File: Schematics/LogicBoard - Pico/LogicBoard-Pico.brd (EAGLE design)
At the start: 104.7 x 99.1 mm, 9 parts

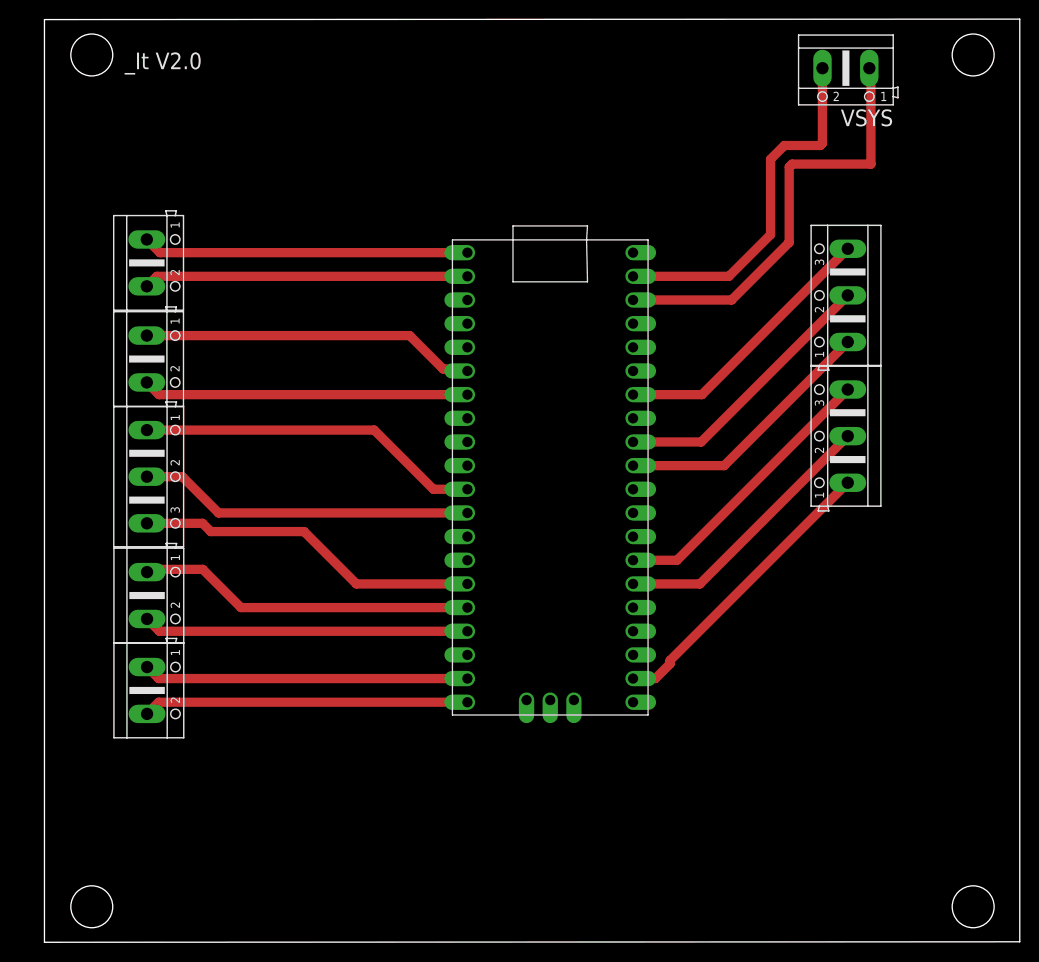
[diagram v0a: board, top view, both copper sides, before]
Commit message: Refactored Power PCB
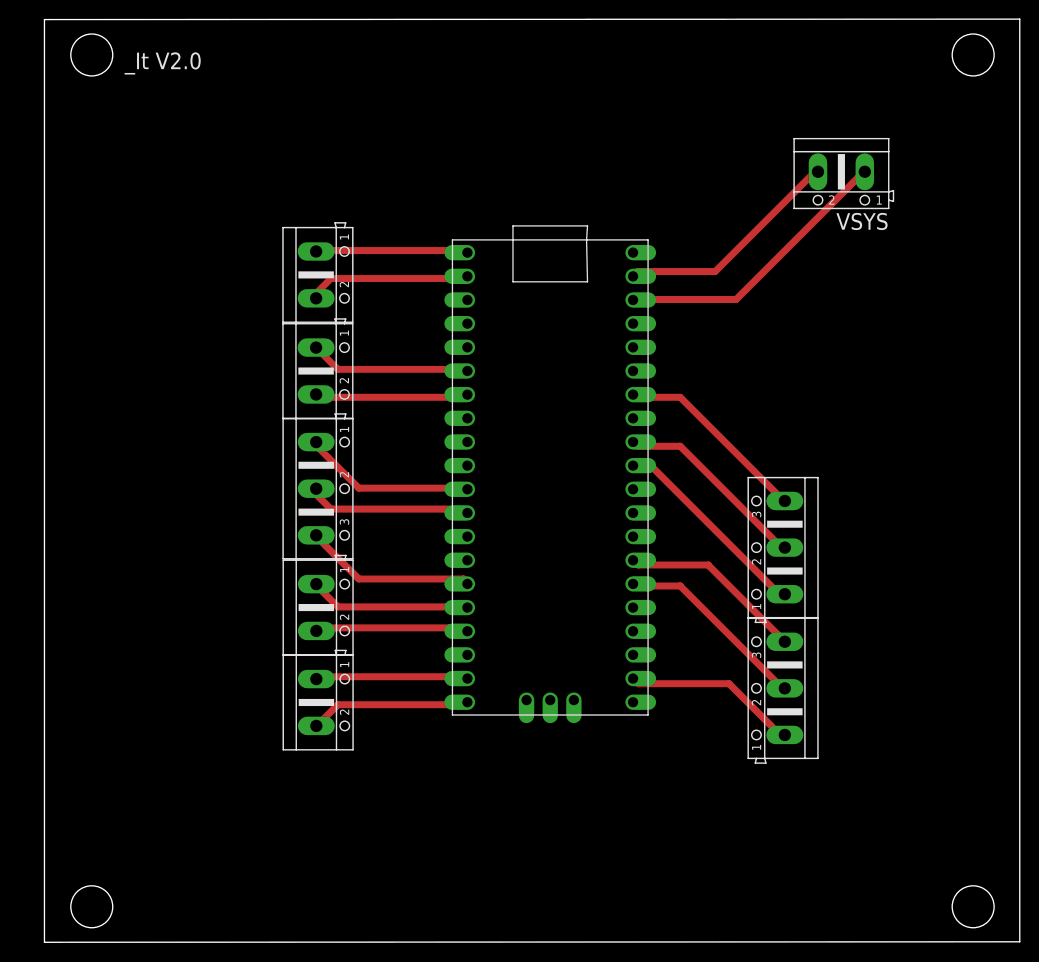
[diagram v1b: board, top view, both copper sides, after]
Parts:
- moved I2C1 27.9 mm to (79.5, 27.3)
- moved ADC 27.9 mm to (79.5, 42.4)
- moved PWM_M1 18.2 mm to (29.2, 25.7)
- moved PWM_M2 18.2 mm to (29.2, 35.9)
- moved PWM_SERVO 18.2 mm to (29.2, 48.7)
- moved I2C0 18.2 mm to (29.2, 61.3)
- moved UART0 18.2 mm to (29.2, 71.6)
- moved VSYS 11.1 mm to (85.6, 82.7)
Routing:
- net N$15: track 36.5 -> 17.3 mm
- net N$10: track 36.0 -> 17.2 mm
- net N$8: track 35.0 -> 16.3 mm
- net N$16: track 37.1 -> 18.5 mm
- net N$18: track 37.0 -> 18.5 mm, vias 0 -> 1
- net N$13: track 34.9 -> 16.5 mm
- net N$11: track 35.0 -> 16.6 mm
- net N$17: track 36.0 -> 17.6 mm
- net N$14: track 34.9 -> 16.6 mm
- net N$12: track 34.9 -> 17.2 mm
- net N$9: track 34.9 -> 17.5 mm
- net N$1: track 46.7 -> 30.5 mm
- net N$2: track 39.1 -> 24.4 mm
- net N$19: track 32.0 -> 18.7 mm
- net N$6: track 30.6 -> 19.9 mm
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
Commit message: Refactored logic board
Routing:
- net N$1: track 30.5 -> 32.4 mm
- added copper zone on layer 16, net N$20
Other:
- board text added: "LOGIC BOARD REV 2 C.C _It Team Designed in GDL,MX."
